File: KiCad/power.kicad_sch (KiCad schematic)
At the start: 15 parts, among them J3 Conn_02x08_Odd_Even, U1 TL072

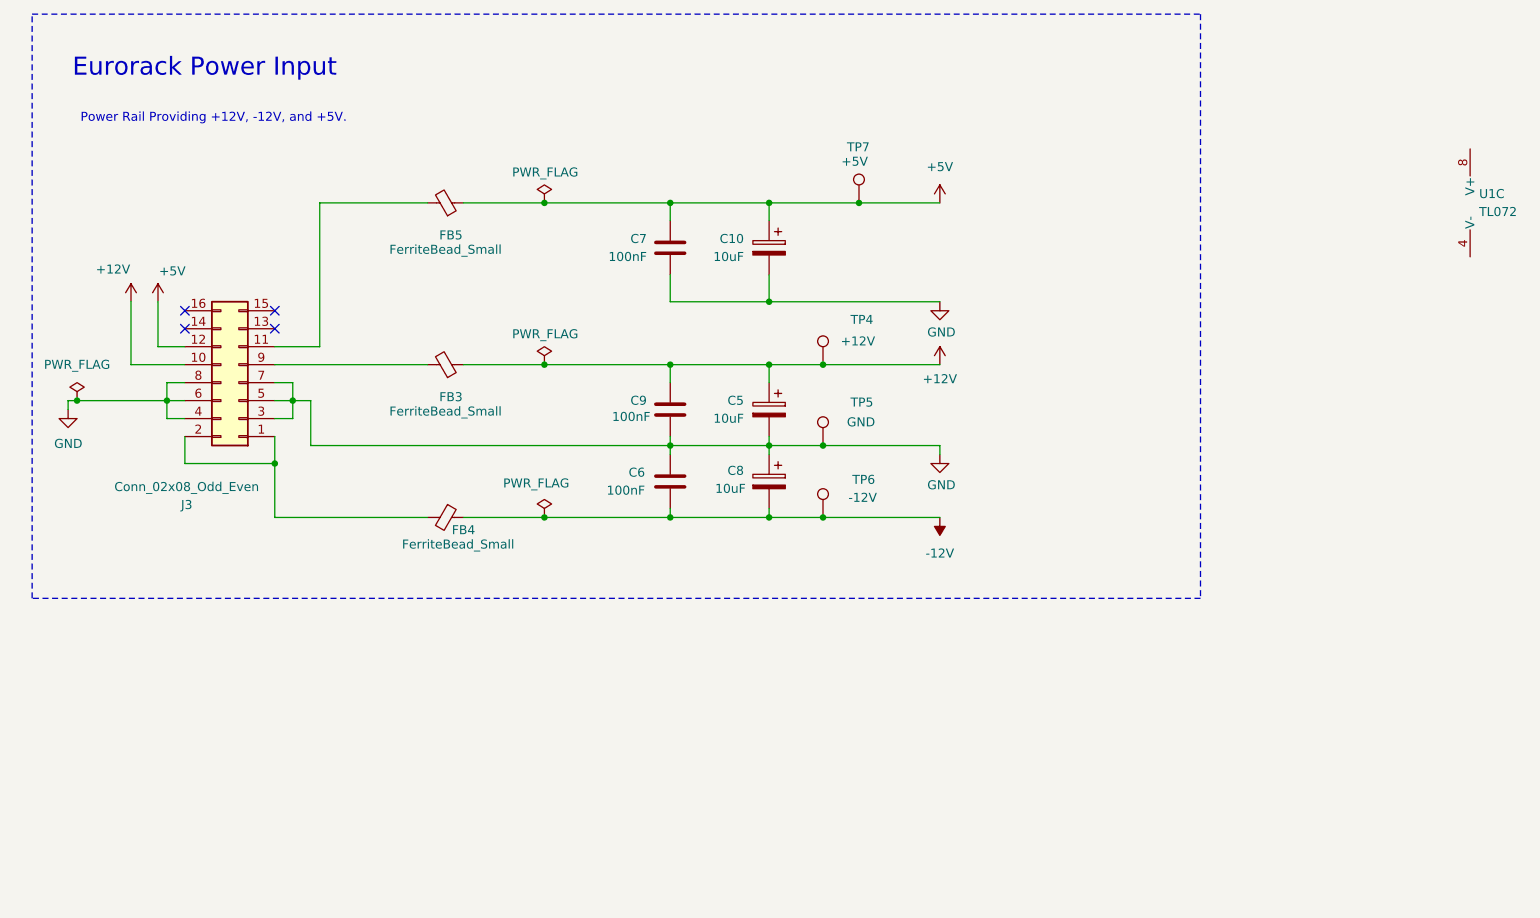
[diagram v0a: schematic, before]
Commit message: feat: rework sequencer switch routing and power sheet
  - add step/output/CV trigger labels and rewired connections
  - replace mode switch with DP3T where needed
  - add power symbols and decoupling parts on the power sheet
  - fix KiCad project metadata and rename the power sheet
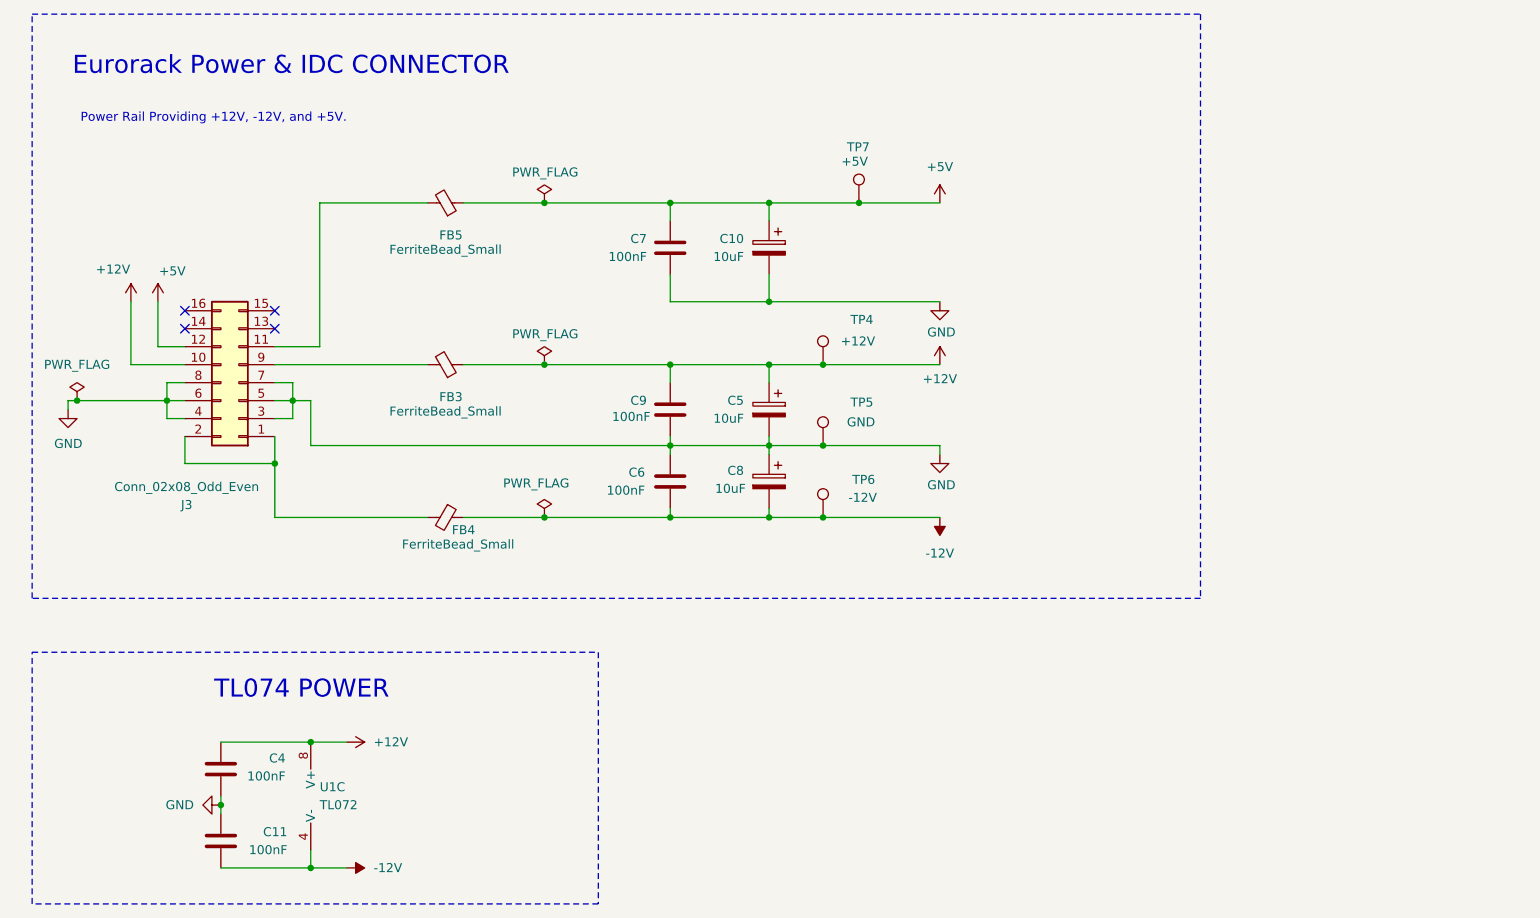
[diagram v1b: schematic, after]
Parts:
- added C11, C4: 100nF, Capacitor_SMD:C_0805_2012Metric_Pad1.18x1.45mm_HandSolder, symbol Device:C
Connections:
- net +12V: now also U1.8 (V+), C4.1
- net -12V: now also U1.4 (V-), C11.2
- net GND: now also C11.1, C4.2
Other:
- note added: "Eurorack Power & IDC CONNECTOR"
- note added: "TL074 POWER"
- note removed: "Eurorack Power Input"
- company: (none) -> Dirty Dream - Nathanael Noir
- title: (none) -> 5 Step Sequencer 
- moved on the sheet: U1C

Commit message: feat(kicad): add +5V bulk decoupling and tidy schematic layout
  - add C13 as a 10uF polarized capacitor across +5V and GND
  - add project title/revision metadata and clearer section labels
  - rename the power sheet to "EURORACK POWER"
  - clean up power-sheet wiring, grounding, and text placement
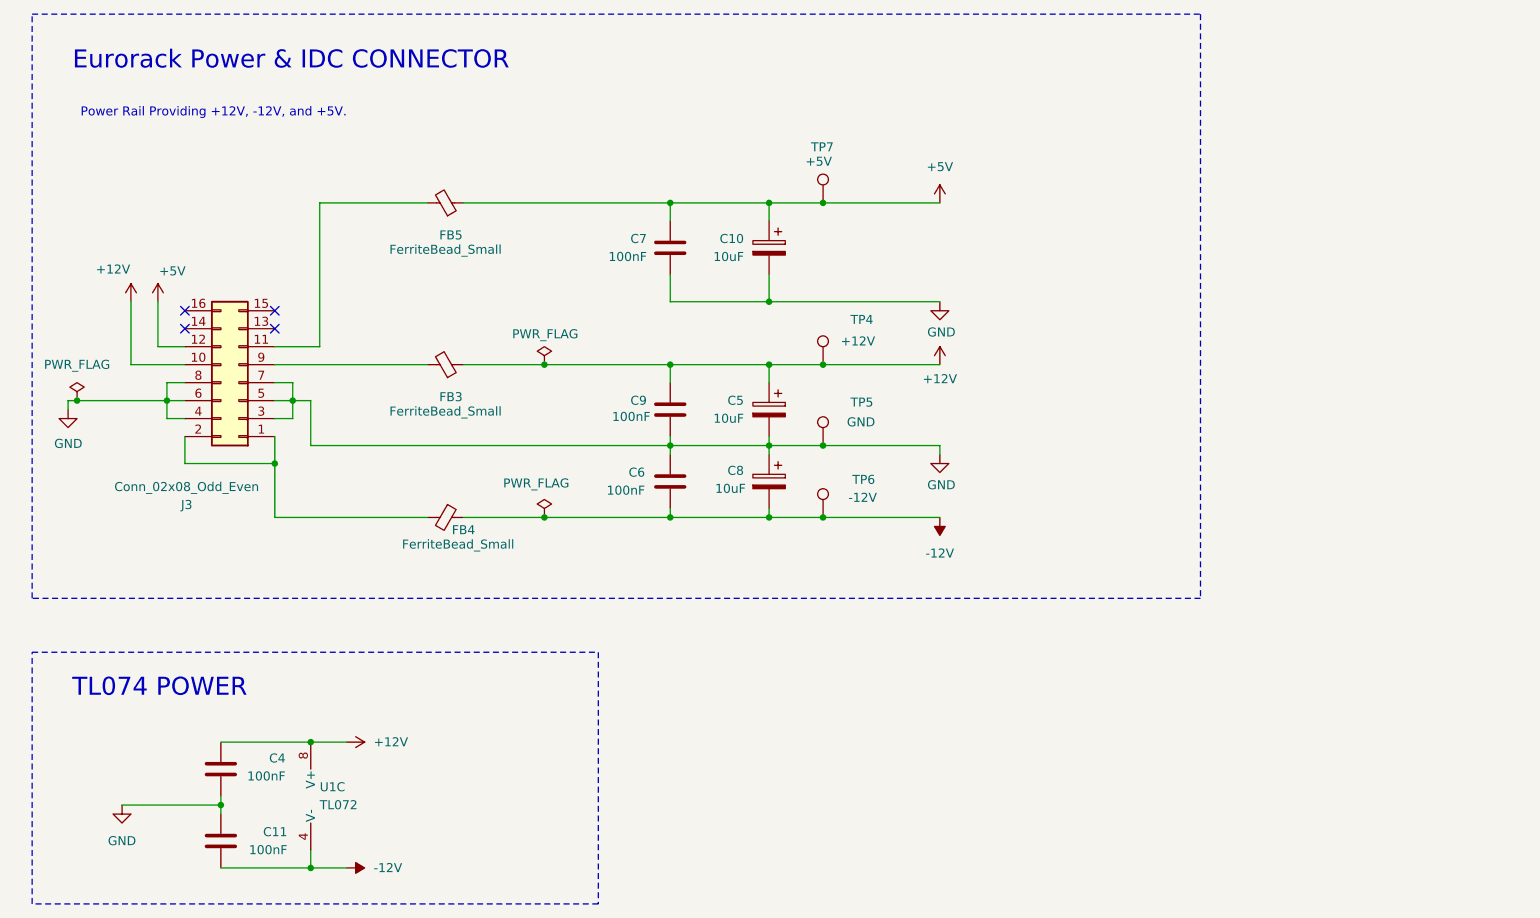
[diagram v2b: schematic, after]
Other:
- title: 5 Step Sequencer  -> 5 Step Sequencer
- moved on the sheet: TP7
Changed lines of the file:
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@@
 	(paper "A4")
 	(title_block
-		(title "5 Step Sequencer ")
+		(title "5 Step Sequencer")
 		(date "2026-03-12")
 		(company "Dirty Dream - Nathanael Noir")
-		(comment 1 "Buchla Inspired")
+		(comment 1 "A 5 step sequencer inspired by the Buchla Sound Easel")
 	)
 	(rectangle
@@
 	(text "TL074 POWER"
 		(exclude_from_sim no)
-		(at 57.15 112.014 0)
+		(at 37.084 111.76 0)
 		(effects
 			(font
@@
 	(text "Eurorack Power & IDC CONNECTOR"
 		(exclude_from_sim no)
-		(at 55.626 23.876 0)
+		(at 55.626 23.114 0)
 		(effects
 			(font
@@
 	(text "Power Rail Providing +12V, -12V, and +5V."
 		(exclude_from_sim no)
-		(at 44.704 31.242 0)
+		(at 44.704 30.48 0)
 		(effects
 			(font
@@
 	)
 	(junction
-		(at 91.44 43.18)
-		(diameter 0)
-		(color 0 0 0 0)
-	)
-	(junction
 		(at 123.19 87.63)
 		(diameter 0)
@@
 	)
 	(junction
+		(at 130.81 43.18)
+		(diameter 0)
+		(color 0 0 0 0)
+	)
+	(junction
 		(at 38.1 71.12)
 		(diameter 0)
@@
 	)
 	(junction
-		(at 135.89 43.18)
-		(diameter 0)
-		(color 0 0 0 0)
-	)
-	(junction
 		(at 109.22 87.63)
 		(diameter 0)
@@
 	(wire
 		(pts
+			(xy 130.81 43.18) (xy 147.32 43.18)
+		)
+		(stroke
+			(width 0)
+			(type default)
+		)
+	)
+	(wire
+		(pts
 			(xy 91.44 87.63) (xy 109.22 87.63)
 		)
@@
 	(wire
 		(pts
-			(xy 109.22 43.18) (xy 123.19 43.18)
-		)
-		(stroke
-			(width 0)
-			(type default)
-		)
-	)
-	(wire
-		(pts
 			(xy 130.81 66.04) (xy 147.32 66.04)
 		)
@@
 	(wire
 		(pts
+			(xy 123.19 43.18) (xy 130.81 43.18)
+		)
+		(stroke
+			(width 0)
+			(type default)
+		)
+	)
+	(wire
+		(pts
 			(xy 91.44 66.04) (xy 109.22 66.04)
 		)
@@
 	(wire
 		(pts
-			(xy 91.44 43.18) (xy 109.22 43.18)
-		)
-		(stroke
-			(width 0)
-			(type default)
-		)
-	)
-	(wire
-		(pts
 			(xy 109.22 76.2) (xy 109.22 77.47)
 		)
@@
 	(wire
 		(pts
+			(xy 123.19 43.18) (xy 109.22 43.18)
+		)
+		(stroke
+			(width 0)
+			(type default)
+		)
+	)
+	(wire
+		(pts
 			(xy 123.19 66.04) (xy 130.81 66.04)
 		)
@@
 	(wire
 		(pts
-			(xy 135.89 43.18) (xy 147.32 43.18)
-		)
-		(stroke
-			(width 0)
-			(type default)
-		)
-	)
-	(wire
-		(pts
-			(xy 80.01 43.18) (xy 91.44 43.18)
+			(xy 80.01 43.18) (xy 109.22 43.18)
 		)
 		(stroke
@@
 	(wire
 		(pts
+			(xy 31.75 128.27) (xy 45.72 128.27)
+		)
+		(stroke
+			(width 0)
+			(type default)
+		)
+	)
+	(wire
+		(pts
 			(xy 53.34 87.63) (xy 53.34 80.01)
 		)
@@
 		(pts
 			(xy 24.13 71.12) (xy 25.4 71.12)
-		)
-		(stroke
-			(width 0)
-			(type default)
-		)
-	)
-	(wire
-		(pts
-			(xy 123.19 43.18) (xy 135.89 43.18)
 		)
 		(stroke
@@
 	(symbol
 		(lib_id "power:GND")
-		(at 45.72 128.27 270)
+		(at 31.75 128.27 0)
 		(unit 1)
 		(exclude_from_sim no)
@@
 		(fields_autoplaced yes)
 		(property "Reference" "#PWR031"
-			(at 39.37 128.27 0)
+			(at 31.75 134.62 0)
 			(effects
 				(font
@@
 		)
 		(property "Value" "GND"
-			(at 41.91 128.2699 90)
-			(effects
-				(font
-					(size 1.27 1.27)
-				)
-				(justify right)
+			(at 31.75 133.35 0)
+			(effects
+				(font
+					(size 1.27 1.27)
+				)
 			)
 		)
 		(property "Footprint" ""
-			(at 45.72 128.27 0)
+			(at 31.75 128.27 0)
 			(effects
 				(font
@@
 		)
 		(property "Datasheet" ""
-			(at 45.72 128.27 0)
+			(at 31.75 128.27 0)
 			(effects
 				(font
@@
 		)
 		(property "Description" "Power symbol creates a global label with name \"GND\" , ground"
-			(at 45.72 128.27 0)
+			(at 31.75 128.27 0)
 			(effects
 				(font
@@
 	(symbol
 		(lib_id "Connector:TestPoint")
-		(at 135.89 43.18 0)
+		(at 130.81 43.18 0)
 		(mirror y)
 		(unit 1)
@@
 		(dnp no)
 		(property "Reference" "TP7"
-			(at 137.414 35.306 0)
+			(at 132.334 35.306 0)
 			(effects
 				(font
@@
 		)
 		(property "Value" "+5V"
-			(at 137.16 37.338 0)
+			(at 132.08 37.338 0)
 			(effects
 				(font
@@
 		)
 		(property "Footprint" "TestPoint:TestPoint_Pad_D1.5mm"
+			(at 125.73 43.18 0)
+			(effects
+				(font
+					(size 1.27 1.27)
+				)
+				(hide yes)
+			)
+		)
+		(property "Datasheet" "~"
+			(at 125.73 43.18 0)
+			(effects
+				(font
+					(size 1.27 1.27)
+				)
+				(hide yes)
+			)
+		)
+		(property "Description" "test point"
 			(at 130.81 43.18 0)
-			(effects
-				(font
-					(size 1.27 1.27)
-				)
-				(hide yes)
-			)
-		)
-		(property "Datasheet" "~"
-			(at 130.81 43.18 0)
-			(effects
-				(font
-					(size 1.27 1.27)
-				)
-				(hide yes)
-			)
-		)
-		(property "Description" "test point"
-			(at 135.89 43.18 0)
 			(effects
 				(font
@@
 					(unit 1)
 				)
-			)
-		)
-	)
-	(symbol
-		(lib_id "power:PWR_FLAG")
-		(at 91.44 43.18 0)
-		(mirror y)
-		(unit 1)
-		(exclude_from_sim no)
-		(in_bom yes)
-		(on_board yes)
-		(dnp no)
-		(property "Reference" "#FLG04"
-			(at 91.44 41.275 0)
-			(effects
-				(font
-					(size 1.27 1.27)
-				)
-				(hide yes)
-			)
-		)
-		(property "Value" "PWR_FLAG"
-			(at 86.868 38.862 0)
-			(effects
-				(font
-					(size 1.27 1.27)
-				)
-				(justify right)
-			)
-		)
-		(property "Footprint" ""
-			(at 91.44 43.18 0)
-			(effects
-				(font
-					(size 1.27 1.27)
-				)
-				(hide yes)
-			)
-		)
-		(property "Datasheet" "~"
-			(at 91.44 43.18 0)
-			(effects
-				(font
-					(size 1.27 1.27)
-				)
-				(hide yes)
-			)
-		)
-		(property "Description" "Special symbol for telling ERC where power comes from"
-			(at 91.44 43.18 0)
-			(effects
-				(font
-					(size 1.27 1.27)
-				)
-				(hide yes)
-			)
-		)
-		(pin "1"
-		)
-		(instances
-			(project "5 Sep Sequencer"
-				(path "/96e48c46-040c-48e5-b6d4-8ee98b2fce0b/4fa43ce6-75e2-4254-9dee-ae44702d62b6"
-					(reference "#FLG04")
-					(unit 1)
-				)

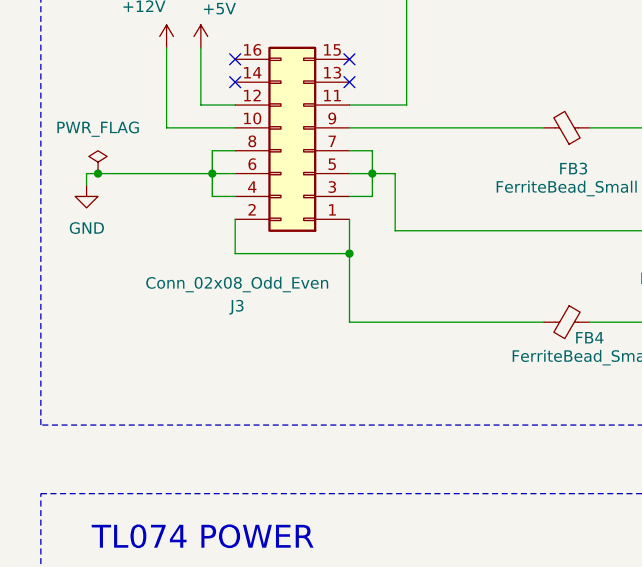
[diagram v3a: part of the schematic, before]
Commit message: adding some missing footprints
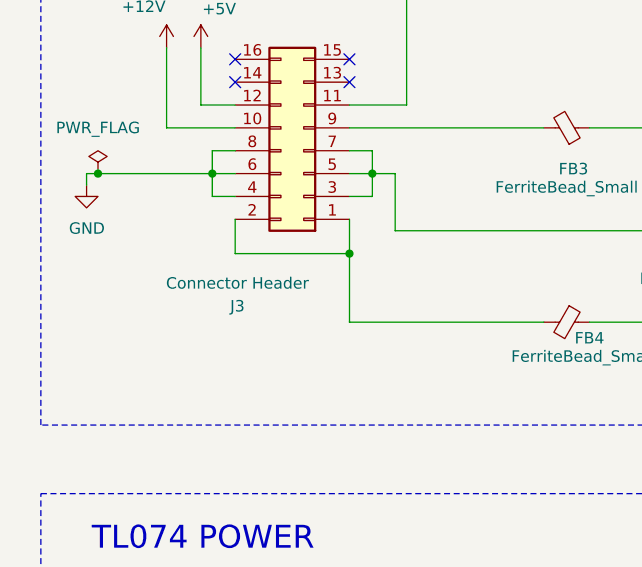
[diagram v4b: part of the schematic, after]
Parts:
- C10, C11, C4, C5, C6, C7, C8, C9, FB3, FB4, FB5, TP4, TP5, TP6, TP7: now left out of the parts list
- J3: value Conn_02x08_Odd_Even -> Connector Header; footprint (none) -> Connector_IDC:IDC-Header_2x08_P2.54mm_Vertical
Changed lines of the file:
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@@
 		(unit 1)
 		(exclude_from_sim no)
-		(in_bom yes)
+		(in_bom no)
 		(on_board yes)
 		(dnp no)
@@
 		(unit 1)
 		(exclude_from_sim no)
-		(in_bom yes)
+		(in_bom no)
 		(on_board yes)
 		(dnp no)
@@
 		(unit 1)
 		(exclude_from_sim no)
-		(in_bom yes)
+		(in_bom no)
 		(on_board yes)
 		(dnp no)
@@
 		(unit 1)
 		(exclude_from_sim no)
-		(in_bom yes)
+		(in_bom no)
 		(on_board yes)
 		(dnp no)
@@
 		(unit 1)
 		(exclude_from_sim no)
-		(in_bom yes)
+		(in_bom no)
 		(on_board yes)
 		(dnp no)
@@
 		(unit 1)
 		(exclude_from_sim no)
-		(in_bom yes)
+		(in_bom no)
 		(on_board yes)
 		(dnp no)
@@
 			)
 		)
-		(property "Value" "Conn_02x08_Odd_Even"
+		(property "Value" "Connector Header"
 			(at 40.894 83.312 0)
 			(effects
@@
 			)
 		)
-		(property "Footprint" ""
+		(property "Footprint" "Connector_IDC:IDC-Header_2x08_P2.54mm_Vertical"
 			(at 48.26 68.58 0)
 			(effects
@@
 		(unit 1)
 		(exclude_from_sim no)
-		(in_bom yes)
+		(in_bom no)
 		(on_board yes)
 		(dnp no)
@@
 		(unit 1)
 		(exclude_from_sim no)
-		(in_bom yes)
+		(in_bom no)
 		(on_board yes)
 		(dnp no)
@@
 		(unit 1)
 		(exclude_from_sim no)
-		(in_bom yes)
+		(in_bom no)
 		(on_board yes)
 		(dnp no)
@@
 		(unit 1)
 		(exclude_from_sim no)
-		(in_bom yes)
+		(in_bom no)
 		(on_board yes)
 		(dnp no)
@@
 		(unit 1)
 		(exclude_from_sim no)
-		(in_bom yes)
+		(in_bom no)
 		(on_board yes)
 		(dnp no)
@@
 		(unit 1)
 		(exclude_from_sim no)
-		(in_bom yes)
+		(in_bom no)
 		(on_board yes)
 		(dnp no)
@@
 		(unit 1)
 		(exclude_from_sim no)
-		(in_bom yes)
+		(in_bom no)
 		(on_board yes)
 		(dnp no)
@@
 		(unit 1)
 		(exclude_from_sim no)
-		(in_bom yes)
+		(in_bom no)
 		(on_board yes)
 		(dnp no)
@@
 		(unit 1)
 		(exclude_from_sim no)
-		(in_bom yes)
-		(on_board yes)
-		(dnp no)
+		(in_bom no)
+		(on_board yes)
+		(dnp no)

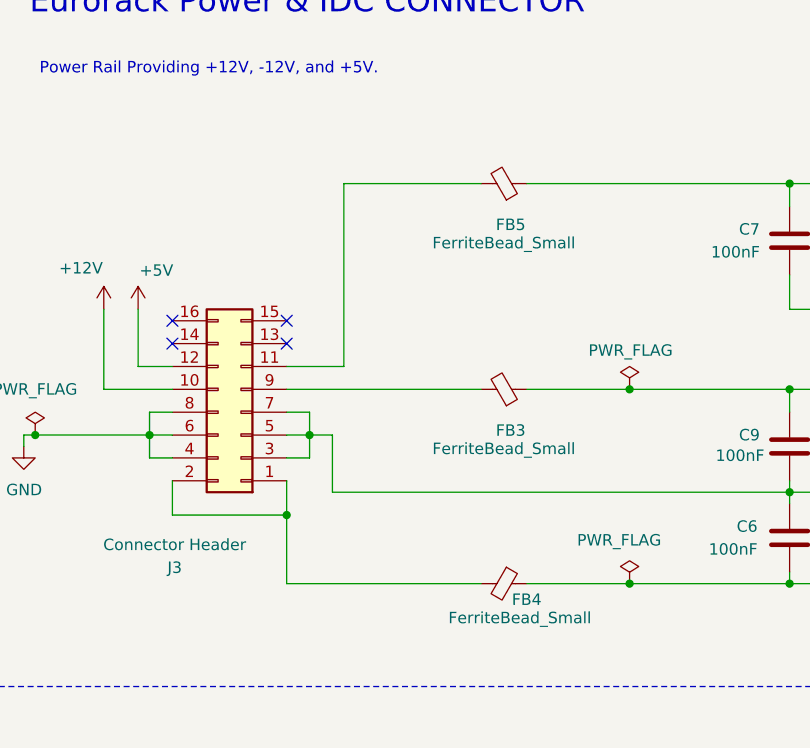
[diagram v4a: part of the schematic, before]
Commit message: Changing Toggle Switch Foorptint
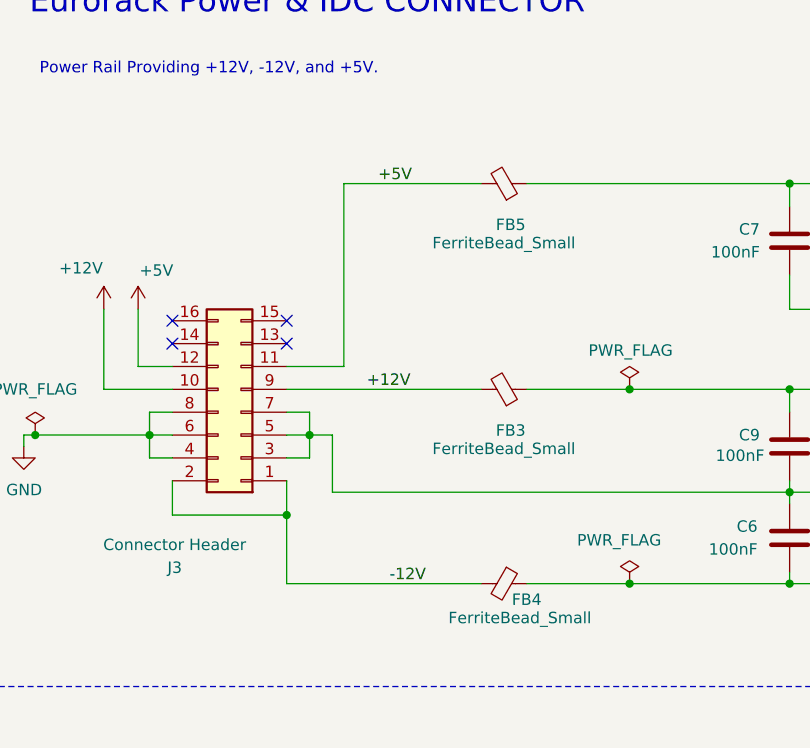
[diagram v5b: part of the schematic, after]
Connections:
- net +12V: now also FB3.2, J3.9 (Pin_9)
- net +5V: now also FB5.2, J3.11 (Pin_11)
- net -12V: now also FB4.2, J3.1 (Pin_1), J3.2 (Pin_2)
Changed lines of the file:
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@@
+		)
+	)
+	(label "-12V"
+		(at 64.77 87.63 0)
+		(effects
+			(font
+				(size 1.27 1.27)
+			)
+			(justify left bottom)
+		)
+	)
+	(label "+5V"
+		(at 63.5 43.18 0)
+		(effects
+			(font
+				(size 1.27 1.27)
+			)
+			(justify left bottom)
+		)
+	)
+	(label "+12V"
+		(at 62.23 66.04 0)
+		(effects
+			(font
+				(size 1.27 1.27)
+			)
+			(justify left bottom)
 		)
 	)

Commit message: adding last missing footprints
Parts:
- U1: footprint (none) -> Package_SO:JEITA_SOIC-8_3.9x4.9mm_P1.27mm; now left out of the parts list
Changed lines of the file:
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@@
 		(unit 3)
 		(exclude_from_sim no)
-		(in_bom yes)
+		(in_bom no)
 		(on_board yes)
 		(dnp no)
@@
 			)
 		)
-		(property "Footprint" ""
+		(property "Footprint" "Package_SO:JEITA_SOIC-8_3.9x4.9mm_P1.27mm"
 			(at 60.96 127 0)
 			(effects

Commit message: new footprint for tl072
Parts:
- U1: footprint Package_SO:JEITA_SOIC-8_3.9x4.9mm_P1.27mm -> Package_SO:SOIC-8_3.9x4.9mm_P1.27mm
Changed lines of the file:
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@@
 			)
 		)
-		(property "Footprint" "Package_SO:JEITA_SOIC-8_3.9x4.9mm_P1.27mm"
+		(property "Footprint" "Package_SO:SOIC-8_3.9x4.9mm_P1.27mm"
 			(at 60.96 127 0)
 			(effects

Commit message: routing
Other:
- note added: "TL072 POWER"
- note removed: "TL074 POWER"
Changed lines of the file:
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@@
 		)
 	)
-	(text "TL074 POWER"
+	(text "TL072 POWER"
 		(exclude_from_sim no)
 		(at 37.084 111.76 0)
